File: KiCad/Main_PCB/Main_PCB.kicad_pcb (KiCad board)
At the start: 4 copper layers, 60 x 16 mm, 44 parts, among them J1 USB_C_Receptacle_USB2.0_14P, J2 Display, Q1 S8050, Q2 S8050, SW3 Main Power, U1 CP2102N-Axx-xQFN28, U2 ESP32-PICO-D4, U3 MCP73831-2-OT, U4 AMS1117

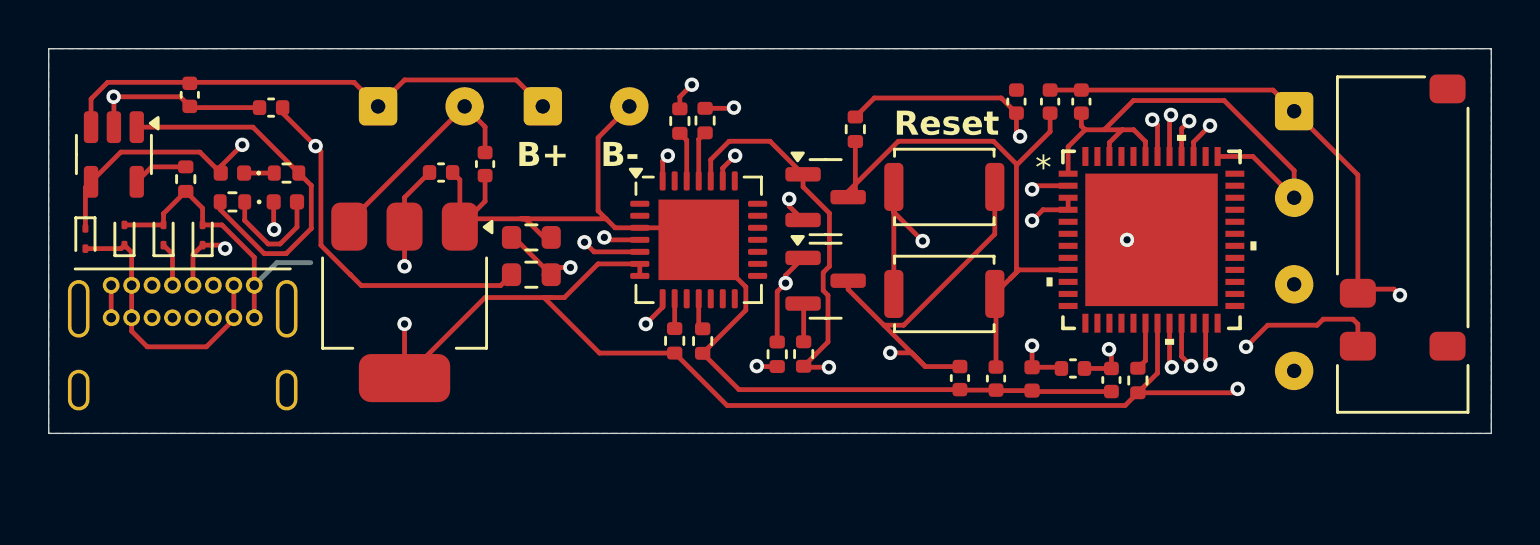
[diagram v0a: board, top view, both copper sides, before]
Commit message: Updated for JLCPCB
- Added BOM
- Changed Diode footprints
- added JLC part numbers
- added cap touch pins
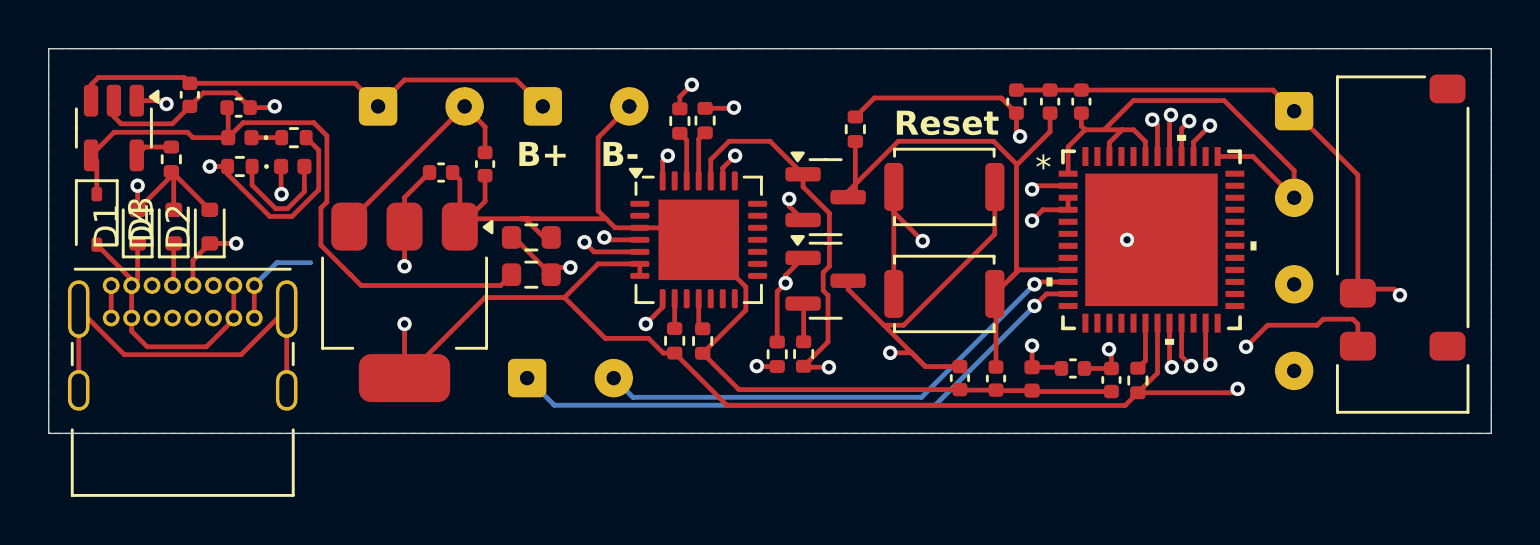
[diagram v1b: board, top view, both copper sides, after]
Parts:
- added J3: Cap Touch, Connector_Wire:SolderWire-0.1sqmm_1x02_P3.6mm_D0.4mm_OD1mm, F.Cu at (135.9, 110.7)
- D1, D2, D4: footprint Diode_SMD:D_SOD-923 -> Diode_SMD:D_SOD-523
- D3: footprint Diode_SMD:D_SOD-923 -> Diode_SMD:D_SOD-323
- moved GREEN1 1.50 mm to (126.2, 101.9)
- moved R12 1.50 mm to (124.0, 101.9)
- moved R13 1.50 mm to (126.2, 100.7)
- moved RED1 1.50 mm to (124.0, 100.7)
- moved C7 1.35 mm to (123.9, 99.5), turned to 180 degrees
- moved U3 1.10 mm to (118.7, 100.3)
- moved R11 1.02 mm to (121.1, 101.6)
- moved D3 0.92 mm to (118.0, 104.1)
- moved D1 0.65 mm to (119.7, 104.4)
- moved D4 0.55 mm to (121.2, 104.4)
- moved D2 0.46 mm to (122.7, 104.4)
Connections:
- U2 pad 10: unconnected-(U2-IO34-Pad10) -> Net-(J3-Pin_2)
- U2 pad 11: unconnected-(U2-IO35-Pad11) -> Net-(J3-Pin_1)
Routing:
- net Net-(J3-Pin_1): track 0.00 -> 24.9 mm, vias 0 -> 1
- net Net-(J3-Pin_2): track 0.00 -> 21.2 mm, vias 0 -> 1
- net unconnected-(J1-SHIELD-PadS1): track 0.00 -> 17.0 mm
- net Net-(U3-STAT): track 15.4 -> 13.1 mm, vias 0 -> 2
- net +3.3V: track 113.2 -> 112.1 mm
- net +5V USB: track 28.3 -> 27.2 mm, vias 2 -> 0
- net Net-(U3-PROG): track 2.30 -> 1.58 mm
- net Net-(D1-A1): track 11.8 -> 12.5 mm
- net Net-(BT1-+): track 21.6 -> 21.0 mm
- net /USB_DN: track 20.7 -> 20.1 mm
- net GND: track 98.5 -> 98.9 mm, vias 5 -> 6
